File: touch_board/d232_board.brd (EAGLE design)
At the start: 100 x 80 mm, 14 parts, among them IC3 7805TV, IC4 7805TV

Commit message: update board
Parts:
- added C1, C3: 0.47, rcl:C1206K
- added C2, C4, C5: 22uf, rcl:C1206K
- added R1, R2, R3, R4, R5, R6, R7, R8: 91, rcl:0204V
- added X1: 057-050-1, con-panduit:057-050-1
- IC1, IC2: value (none) -> uln2803
- moved JP1 22.9 mm to (20.3, 12.7), turned to 90 degrees
- moved SG2 18.0 mm to (44.5, 14.0)
- moved SG3 16.9 mm to (97.8, 14.0)
- moved SG1 15.5 mm to (68.6, 14.0)
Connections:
- new net N$28: JP6.1, X1.1
- new net N$29: JP6.2, X1.2
- new net N$30: JP6.3, X1.3
- new net N$31: JP6.4, X1.4
- new net N$32: JP2.1, R1.1
- new net N$33: JP2.2, R2.1
- new net N$34: JP2.3, R3.1
- new net N$35: JP2.4, R4.1
- new net N$36: JP2.5, R5.1
- new net N$37: JP2.6, R6.1
- new net N$38: JP2.7, R7.1
- new net N$39: JP2.8, R8.1
- net +10V: now also C4.1
- net +24V: now also C1.1, C3.1
- net +5V: now also C2.1, C5.1, R1.2, R2.2, R3.2, R4.2, R5.2, R6.2, R7.2, R8.2
- net GND: now also C1.2, C2.2, C3.2, C4.2, C5.2, JP6.10, X1.50
- net N$10: now also X1.10
- net N$11: now also X1.11
- net N$14: now also X1.14
- net N$16: now also X1.16
- net N$17: now also X1.17
- net N$18: now also X1.18
- net N$20: now also X1.20
- net N$21: now also X1.21
- net N$9: now also X1.9
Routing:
- net GND: track 101.6 -> 204.9 mm, vias 0 -> 1
- net N$16: track 9.05 -> 61.2 mm
- net N$29: track 0.00 -> 46.3 mm
- net N$14: track 8.96 -> 53.3 mm
- net N$30: track 0.00 -> 43.5 mm
- net N$31: track 0.00 -> 43.5 mm
- net N$28: track 0.00 -> 40.0 mm
- net +10V: track 82.3 -> 121.6 mm, vias 0 -> 1
- net N$1: track 7.62 -> 46.8 mm
- net +5V: track 91.1 -> 130.1 mm
- net N$2: track 7.82 -> 43.2 mm
- net N$11: track 8.96 -> 43.0 mm
- net N$3: track 7.72 -> 39.7 mm
- net N$17: track 10.3 -> 42.0 mm
- net N$18: track 10.2 -> 41.3 mm
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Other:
- board size 100 x 80 mm -> 116.5 x 80 mm

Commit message: up
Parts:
- added IC5: 7805TV, linear:TO220V
- added R9: 91, rcl:0204V
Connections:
- new net +12V: C3.1, IC4.1, IC5.3
- net +24V: now also IC5.1; no longer C3.1, IC4.1
- net +5V: now also R9.2
- net GND: now also IC5.2
- net N$29: now also R9.1
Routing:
- net +12V: track 0.00 -> 85.2 mm, vias 0 -> 1
- net +5V: track 130.1 -> 149.9 mm
- net GND: track 204.9 -> 223.2 mm, vias 1 -> 0
- net +24V: track 190.1 -> 199.9 mm
- net N$29: track 46.3 -> 39.9 mm
- net N$31: track 43.5 -> 48.4 mm
- net N$30: track 43.5 -> 46.8 mm

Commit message: up
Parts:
- removed IC4: 7805TV, linear:TO220V
- added C6, C7: 0.47, rcl:C1206K
- added C8: 22uf, rcl:C1206K
- added IC4_10V: 7805TV, linear:TO220V
- added LED1: PWR, led:CHIPLED_1206
- added R10: 91, rcl:0204V
- added R11: 1k, rcl:0204V
- JP1: value (none) -> LEDC
- JP2: value (none) -> LEDP
- JP3: value (none) -> PORTIO
- JP4: value (none) -> PORT2
- JP5: value (none) -> PORT3
- JP6: value (none) -> PORT1
- JP7: value (none) -> DC POWER
- moved IC1 36.9 mm to (64.8, 43.2)
- moved JP4 36.9 mm to (63.5, 55.9)
- moved C1 35.7 mm to (54.6, 62.2)
- moved C2 35.7 mm to (62.2, 62.2)
- moved R9 32.5 mm to (40.6, 47.0), turned to 90 degrees
- moved JP6 30.3 mm to (31.8, 55.9), turned to 180 degrees
- moved JP7 16.5 mm to (31.8, 69.8)
- moved JP5 15.5 mm to (92.7, 55.9)
- moved IC2 15.3 mm to (94.0, 43.2)
- moved SG1 4.58 mm to (71.1, 10.2)
- moved SG2 4.58 mm to (41.9, 10.2)
- moved C4 4.02 mm to (83.8, 62.2)
- moved C3 4.02 mm to (76.2, 62.2)
- moved SG3 4.02 mm to (99.1, 10.2)
- moved JP3 3.81 mm to (6.35, 62.2)
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- renumbered IC3 to IC3_5V, IC5 to IC5_12V
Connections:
- new net N$40: IC2.15, JP3.2
- new net N$41: IC2.14, JP3.3
- new net N$42: IC2.13, JP3.4
- new net N$43: IC2.12, JP3.5
- new net N$44: IC2.11, JP3.6
- new net N$45: IC2.10, JP3.7
- new net N$46: LED1.A, R11.1
- net +10V: now also IC4_10V.3; no longer IC4.3
- net +12V: now also C8.1, IC4_10V.1, JP7.8; no longer IC4.1
- net +24V: now also C7.1, JP3.1
- net +5V: now also C6.1, R10.2, R11.2
- net GND: now also C6.2, C7.2, C8.2, IC4_10V.2, JP1.9, JP2.9, JP3.8, LED1.C; no longer IC4.2
- net N$30: now also R10.1
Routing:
- net N$40: track 0.00 -> 135.4 mm
- net N$41: track 0.00 -> 130.8 mm
- net N$42: track 0.00 -> 127.0 mm, vias 0 -> 1
- net N$43: track 0.00 -> 121.3 mm, vias 0 -> 1
- net N$44: track 0.00 -> 118.2 mm
- net N$45: track 0.00 -> 112.5 mm
- net GND: track 223.2 -> 331.3 mm
- net +24V: track 199.9 -> 245.0 mm
- net N$16: track 61.2 -> 26.8 mm
- net N$14: track 53.3 -> 24.7 mm
- net N$5: track 32.4 -> 60.3 mm
- net N$4: track 36.0 -> 63.7 mm
- net N$3: track 39.7 -> 66.3 mm
- net N$1: track 46.8 -> 73.0 mm
- net N$2: track 43.2 -> 69.3 mm, vias 0 -> 1
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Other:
- board size 116.5 x 80 mm -> 120.3 x 91.4 mm

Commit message: add board design files
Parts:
- added TP1, TP2, TP3, TP4, TP5, TP6: TPB2,54, testpad:B2,54
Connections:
- net +5V: now also TP3.TP, TP5.TP
- net GND: now also TP4.TP, TP6.TP
- net N$28: now also TP1.TP
- net N$31: now also TP2.TP
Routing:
- net GND: track 331.3 -> 94.7 mm
- net +5V: track 175.6 -> 220.3 mm, vias 1 -> 0
- net N$41: track 130.8 -> 170.0 mm
- net N$31: track 29.4 -> 57.4 mm
- net N$44: track 118.2 -> 95.6 mm, vias 0 -> 2
- net N$40: track 135.4 -> 156.1 mm, vias 0 -> 1
- net N$28: track 28.6 -> 48.8 mm, vias 0 -> 1
- net N$45: track 112.5 -> 96.1 mm, vias 0 -> 1
- net N$10: track 37.2 -> 51.8 mm
- net N$43: track 121.3 -> 106.8 mm
- net N$25: track 53.0 -> 66.0 mm
- net N$26: track 81.5 -> 93.7 mm
- net +12V: track 77.0 -> 87.7 mm
- net +24V: track 245.0 -> 255.3 mm, vias 0 -> 2
- net N$6: track 52.4 -> 60.2 mm
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- added copper zone on layer 16, net GND
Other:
- board text added: "FGB@MCHP V1.0"
- board text added: "Sound and Lightshow board"

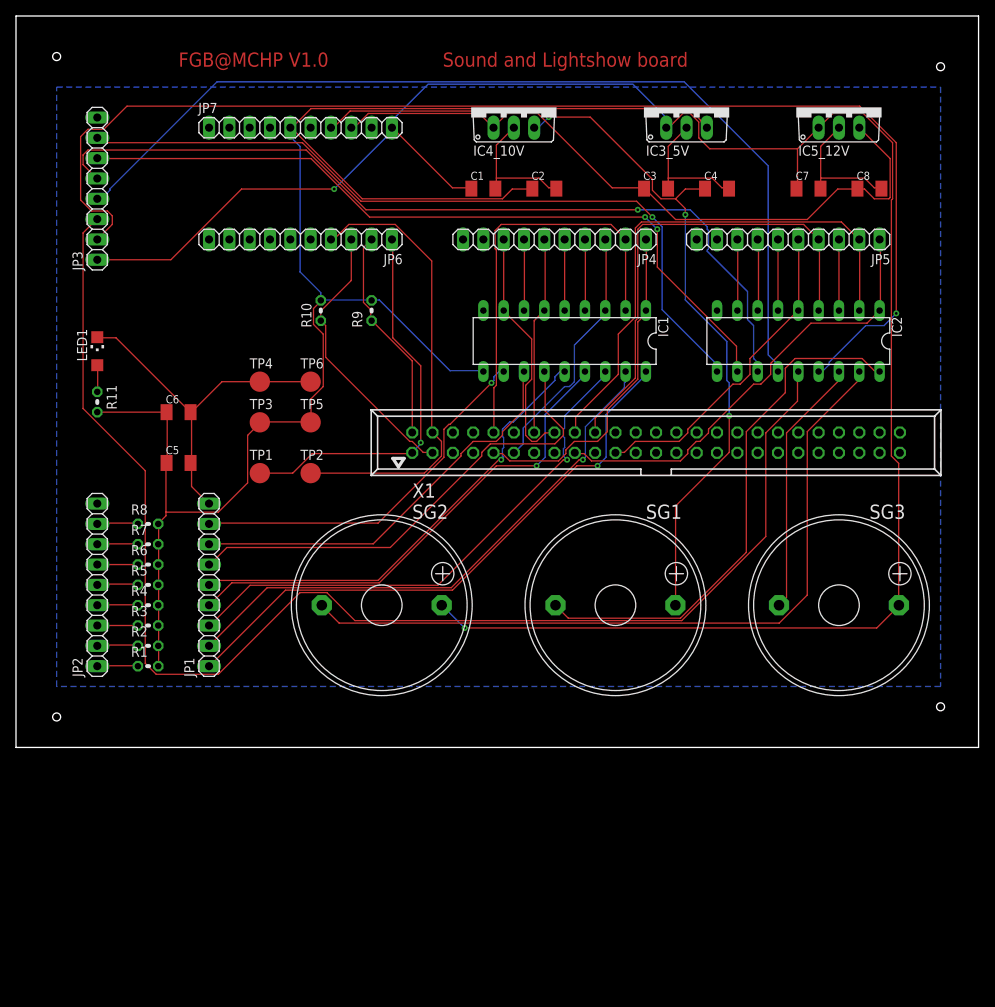
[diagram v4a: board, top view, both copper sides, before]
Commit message: fix missing traces to conector
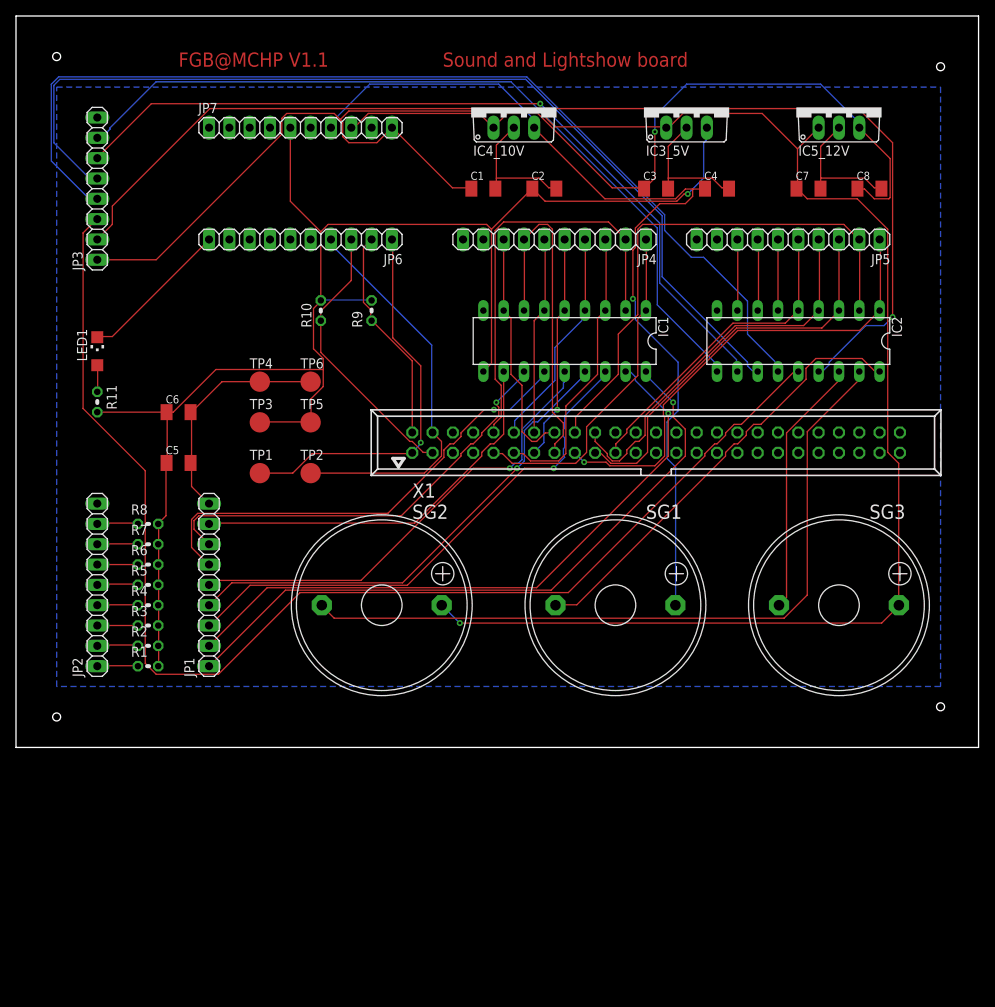
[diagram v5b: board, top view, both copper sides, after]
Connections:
- net N$12: now also X1.12
- net N$13: now also X1.13
- net N$15: now also X1.15
- net N$19: now also X1.19
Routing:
- net N$19: track 8.89 -> 50.5 mm
- net N$15: track 8.91 -> 42.5 mm
- net +5V: track 220.3 -> 192.8 mm, vias 0 -> 1
- net N$13: track 8.89 -> 28.2 mm, vias 0 -> 1
- net N$12: track 8.91 -> 27.9 mm
- net N$43: track 106.8 -> 122.6 mm, vias 1 -> 0
- net N$40: track 156.1 -> 143.3 mm
- net N$41: track 170.0 -> 157.7 mm
- net N$20: track 60.2 -> 48.7 mm
- net N$2: track 69.6 -> 80.4 mm
- net N$25: track 66.0 -> 55.3 mm
- net N$1: track 73.2 -> 83.0 mm
- net +12V: track 87.7 -> 97.3 mm, vias 0 -> 1
- net N$31: track 57.4 -> 50.0 mm
- net N$42: track 120.6 -> 127.8 mm
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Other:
- board text added: "FGB@MCHP V1.1"
- board text removed: "FGB@MCHP V1.0"

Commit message: up
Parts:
- added TP10, TP11, TP7, TP8: TPB2,54, testpad:B2,54
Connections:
- net +10V: now also TP8.TP
- net +12V: now also TP10.TP
- net +24V: now also TP11.TP
- net +5V: now also TP7.TP
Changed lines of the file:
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@@
 <attribute name="VALUE" x="31.75" y="36.703" size="0.0254" layer="27"/>
+</element>
+<element name="TP7" library="testpad" library_urn="urn:adsk.eagle:library:385" package="B2,54" package3d_urn="urn:adsk.eagle:package:27948/1" value="TPB2,54" x="-1.27" y="-11.43" smashed="yes">
+<attribute name="NAME" x="-2.54" y="-9.779" size="1.27" layer="25" ratio="10"/>
+<attribute name="POPULARITY" value="3" x="-1.27" y="-11.43" size="1.778" layer="27" display="off"/>
+<attribute name="TP_SIGNAL_NAME" value="" x="-1.27" y="-11.43" size="1.778" layer="27" display="off"/>
+<attribute name="VALUE" x="-2.54" y="-12.827" size="0.0254" layer="27"/>
+</element>
+<element name="TP8" library="testpad" library_urn="urn:adsk.eagle:library:385" package="B2,54" package3d_urn="urn:adsk.eagle:package:27948/1" value="TPB2,54" x="-1.27" y="-17.78" smashed="yes">
+<attribute name="NAME" x="-2.54" y="-16.129" size="1.27" layer="25" ratio="10"/>
+<attribute name="POPULARITY" value="3" x="-1.27" y="-17.78" size="1.778" layer="27" display="off"/>
+<attribute name="TP_SIGNAL_NAME" value="" x="-1.27" y="-17.78" size="1.778" layer="27" display="off"/>
+<attribute name="VALUE" x="-2.54" y="-19.177" size="0.0254" layer="27"/>
+</element>
+<element name="TP10" library="testpad" library_urn="urn:adsk.eagle:library:385" package="B2,54" package3d_urn="urn:adsk.eagle:package:27948/1" value="TPB2,54" x="-1.27" y="-30.48" smashed="yes">
+<attribute name="NAME" x="-2.54" y="-28.829" size="1.27" layer="25" ratio="10"/>
+<attribute name="POPULARITY" value="3" x="-1.27" y="-30.48" size="1.778" layer="27" display="off"/>
+<attribute name="TP_SIGNAL_NAME" value="" x="-1.27" y="-30.48" size="1.778" layer="27" display="off"/>
+<attribute name="VALUE" x="-2.54" y="-31.877" size="0.0254" layer="27"/>
+</element>
+<element name="TP11" library="testpad" library_urn="urn:adsk.eagle:library:385" package="B2,54" package3d_urn="urn:adsk.eagle:package:27948/1" value="TPB2,54" x="-1.27" y="-36.83" smashed="yes">
+<attribute name="NAME" x="-2.54" y="-35.179" size="1.27" layer="25" ratio="10"/>
+<attribute name="POPULARITY" value="3" x="-1.27" y="-36.83" size="1.778" layer="27" display="off"/>
+<attribute name="TP_SIGNAL_NAME" value="" x="-1.27" y="-36.83" size="1.778" layer="27" display="off"/>
+<attribute name="VALUE" x="-2.54" y="-38.227" size="0.0254" layer="27"/>
 </element>
 </elements>
@@
 <wire x1="34.29" y1="56.8452" x2="35.2044" y2="57.7596" width="0.1524" layer="1"/>
 <via x="80.1624" y="61.5696" extent="1-16" drill="0.35"/>
+<contactref element="TP7" pad="TP"/>
+<wire x1="-1.27" y1="-11.43" x2="13.97" y2="2.54" width="0" layer="19" extent="1-1"/>
 </signal>
 <signal name="+10V">
@@
 <wire x1="78.6384" y1="10.2108" x2="78.613" y2="10.16" width="0.1524" layer="16"/>
 <via x="73.3044" y="48.4632" extent="1-16" drill="0.35"/>
+<contactref element="TP8" pad="TP"/>
+<wire x1="-1.27" y1="-17.78" x2="78.613" y2="10.16" width="0" layer="19" extent="1-1"/>
 </signal>
 <signal name="+24V">
@@
 <wire x1="93.8784" y1="62.1792" x2="93.75" y2="62.23" width="0.1524" layer="1"/>
 <via x="51.6636" y="7.9248" extent="1-16" drill="0.35"/>
+<contactref element="TP11" pad="TP"/>
+<wire x1="-1.27" y1="-36.83" x2="49.403" y2="10.16" width="0" layer="19" extent="1-1"/>
 </signal>
 <signal name="N$1">
@@
 <wire x1="74.8284" y1="62.3316" x2="74.7" y2="62.23" width="0.1524" layer="1"/>
 <via x="76.0476" y="69.342" extent="1-16" drill="0.35"/>
+<contactref element="TP10" pad="TP"/>
+<wire x1="-1.27" y1="-30.48" x2="38.1" y2="69.85" width="0" layer="19" extent="1-1"/>
 </signal>
 <signal name="N$40">

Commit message: up
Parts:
- moved TP11 108.2 mm to (39.4, 63.5)
- moved TP10 100.5 mm to (34.3, 63.5)
- moved TP8 85.2 mm to (24.1, 63.5)
- moved TP7 77.6 mm to (19.1, 63.5)
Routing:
- net +5V: track 192.8 -> 238.4 mm, vias 1 -> 0
- net N$41: track 157.7 -> 124.7 mm, vias 0 -> 1
- net N$40: track 143.3 -> 168.0 mm, vias 1 -> 0
- net N$2: track 80.4 -> 69.0 mm
- net N$25: track 55.3 -> 66.2 mm, vias 0 -> 1
- net N$44: track 101.9 -> 111.4 mm, vias 1 -> 0
- net +10V: track 116.8 -> 124.9 mm, vias 1 -> 2
- net +12V: track 97.3 -> 104.9 mm
- net N$20: track 48.7 -> 53.5 mm
- net +24V: track 251.9 -> 255.2 mm, vias 1 -> 3
- net N$13: track 28.2 -> 30.2 mm
- net N$21: track 40.0 -> 41.5 mm
- net N$1: track 83.0 -> 81.8 mm
- net N$3: track 66.2 -> 65.2 mm
- net N$16: track 30.0 -> 30.6 mm

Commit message: up
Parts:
- renumbered SG1 to MSE14LCH2, SG2 to MSE28LWH1, SG3 to MSE28LDD7
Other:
- board text added: "chirp"
- board text added: "siren"
- board text added: "warp"
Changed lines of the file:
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@@
 <text x="16.51" y="77.47" size="1.778" layer="1" font="vector" ratio="15">FGB@MCHP V1.1</text>
 <text x="49.53" y="77.47" size="1.778" layer="1" font="vector" ratio="15" distance="15">Sound and Lightshow board</text>
+<text x="68.58" y="-3.81" size="1.778" layer="1" font="vector" ratio="15" distance="35">chirp</text>
+<text x="96.52" y="-3.81" size="1.778" layer="1" font="vector" ratio="15" distance="35">warp</text>
+<text x="39.37" y="-3.81" size="1.778" layer="1" font="vector" ratio="15" distance="35">siren</text>
 </plain>
 <attributes>
@@
 <attribute name="VALUE" x="19.05" y="66.675" size="1.27" layer="27"/>
 </element>
-<element name="SG1" library="buzzer" library_urn="urn:adsk.eagle:library:113" package="EB2209A" package3d_urn="urn:adsk.eagle:package:5276/1" value="EB2209A" x="71.12" y="10.16" smashed="yes">
+<element name="MSE14LCH2" library="buzzer" library_urn="urn:adsk.eagle:library:113" package="EB2209A" package3d_urn="urn:adsk.eagle:package:5276/1" value="EB2209A" x="71.12" y="10.16" smashed="yes">
 <attribute name="MF" value="" x="95.25" y="-1.27" size="1.778" layer="27" display="off"/>
 <attribute name="MPN" value="" x="95.25" y="-1.27" size="1.778" layer="27" display="off"/>
-<attribute name="NAME" x="74.93" y="20.955" size="1.778" layer="25" ratio="10"/>
+<attribute name="NAME" x="74.93" y="22.225" size="1.778" layer="25" ratio="10"/>
 <attribute name="OC_FARNELL" value="unknown" x="95.25" y="-1.27" size="1.778" layer="27" display="off"/>
 <attribute name="OC_NEWARK" value="unknown" x="95.25" y="-1.27" size="1.778" layer="27" display="off"/>
 <attribute name="VALUE" x="66.04" y="2.54" size="1.778" layer="27" ratio="10"/>
 </element>
-<element name="SG2" library="buzzer" library_urn="urn:adsk.eagle:library:113" package="EB2209A" package3d_urn="urn:adsk.eagle:package:5276/1" value="EB2209A" x="41.91" y="10.16" smashed="yes">
+<element name="MSE28LWH1" library="buzzer" library_urn="urn:adsk.eagle:library:113" package="EB2209A" package3d_urn="urn:adsk.eagle:package:5276/1" value="EB2209A" x="41.91" y="10.16" smashed="yes">
 <attribute name="MF" value="" x="88.9" y="-1.27" size="1.778" layer="27" display="off"/>
 <attribute name="MPN" value="" x="88.9" y="-1.27" size="1.778" layer="27" display="off"/>
-<attribute name="NAME" x="45.72" y="20.955" size="1.778" layer="25" ratio="10"/>
+<attribute name="NAME" x="49.53" y="20.955" size="1.778" layer="25" ratio="10"/>
 <attribute name="OC_FARNELL" value="unknown" x="88.9" y="-1.27" size="1.778" layer="27" display="off"/>
 <attribute name="OC_NEWARK" value="unknown" x="88.9" y="-1.27" size="1.778" layer="27" display="off"/>
 <attribute name="VALUE" x="36.83" y="2.54" size="1.778" layer="27" ratio="10"/>
 </element>
-<element name="SG3" library="buzzer" library_urn="urn:adsk.eagle:library:113" package="EB2209A" package3d_urn="urn:adsk.eagle:package:5276/1" value="EB2209A" x="99.06" y="10.16" smashed="yes">
+<element name="MSE28LDD7" library="buzzer" library_urn="urn:adsk.eagle:library:113" package="EB2209A" package3d_urn="urn:adsk.eagle:package:5276/1" value="EB2209A" x="99.06" y="10.16" smashed="yes">
 <attribute name="MF" value="" x="123.19" y="-26.67" size="1.778" layer="27" display="off"/>
 <attribute name="MPN" value="" x="123.19" y="-26.67" size="1.778" layer="27" display="off"/>
-<attribute name="NAME" x="102.87" y="20.955" size="1.778" layer="25" ratio="10"/>
+<attribute name="NAME" x="99.06" y="22.225" size="1.778" layer="25" ratio="10"/>
 <attribute name="OC_FARNELL" value="unknown" x="123.19" y="-26.67" size="1.778" layer="27" display="off"/>
 <attribute name="OC_NEWARK" value="unknown" x="123.19" y="-26.67" size="1.778" layer="27" display="off"/>
@@
 <signal name="+10V">
 <contactref element="IC4_10V" pad="3"/>
-<contactref element="SG1" pad="+"/>
+<contactref element="MSE14LCH2" pad="+"/>
 <contactref element="JP7" pad="7"/>
 <contactref element="C4" pad="1"/>
@@
 <contactref element="IC3_5V" pad="1"/>
 <contactref element="JP7" pad="10"/>
-<contactref element="SG2" pad="+"/>
-<contactref element="SG3" pad="+"/>
+<contactref element="MSE28LWH1" pad="+"/>
+<contactref element="MSE28LDD7" pad="+"/>
 <contactref element="C1" pad="1"/>
 <contactref element="IC5_12V" pad="1"/>
@@
 <signal name="N$25">
 <contactref element="IC2" pad="18"/>
-<contactref element="SG1" pad="-"/>
+<contactref element="MSE14LCH2" pad="-"/>
 <wire x1="104.0892" y1="38.2524" x2="104.0892" y2="39.3192" width="0.1524" layer="1"/>
 <wire x1="97.536" y1="31.6992" x2="104.0892" y2="38.2524" width="0.1524" layer="1"/>
@@
 <signal name="N$26">
 <contactref element="IC2" pad="17"/>
-<contactref element="SG2" pad="-"/>
+<contactref element="MSE28LWH1" pad="-"/>
 <wire x1="101.4984" y1="38.2524" x2="101.4984" y2="39.3192" width="0.1524" layer="1"/>
 <wire x1="95.0976" y1="31.8516" x2="101.4984" y2="38.2524" width="0.1524" layer="1"/>
@@
 <signal name="N$27">
 <contactref element="IC2" pad="16"/>
-<contactref element="SG3" pad="-"/>
+<contactref element="MSE28LDD7" pad="-"/>
 <wire x1="99.06" y1="38.2524" x2="99.06" y2="39.37" width="0.1524" layer="1"/>
 <wire x1="92.5068" y1="31.6992" x2="99.06" y2="38.2524" width="0.1524" layer="1"/>
